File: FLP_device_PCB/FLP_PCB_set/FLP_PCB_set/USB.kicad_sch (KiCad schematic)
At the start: 2 parts, among them J1 USB_C_Receptacle_USB2.0_16P, U10 USBLC6-2P6

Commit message: FLP_set add
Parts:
- added C42: 22uF, Capacitor_SMD:C_0805_2012Metric, symbol Device:C
- J6: renamed from J1; footprint (none) -> 12402012E212A:AMPHENOL_12402012E212A
- renumbered U10 to U8
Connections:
- net 3.3V_USB: now also U8.5 (VBUS); no longer J6.A4_B9 (VBUS), J6.A9 (VBUS), J6.B4 (VBUS), J6.B4_A9 (VBUS), J6.B9 (VBUS)
- net GND: now also U8.2 (GND), C42.1
- new net 5V_USB: C42.2, J6.A4_B9 (VBUS), J6.A9 (VBUS), J6.B4 (VBUS), J6.B4_A9 (VBUS), J6.B9 (VBUS)

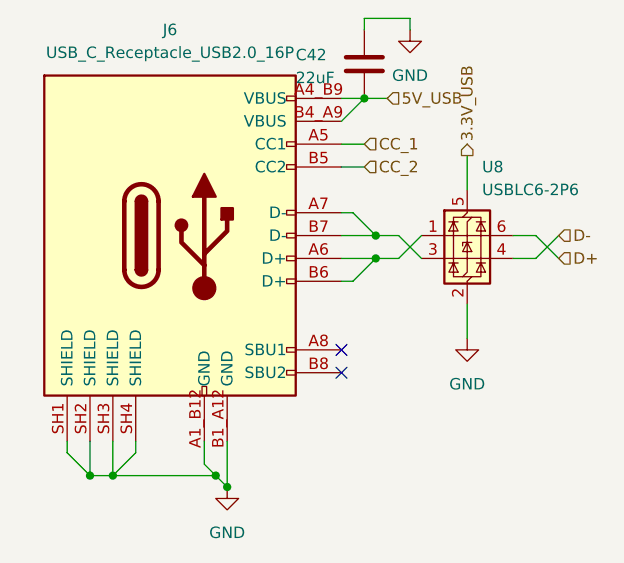
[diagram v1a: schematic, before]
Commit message: PCB fixing end adding description pdf
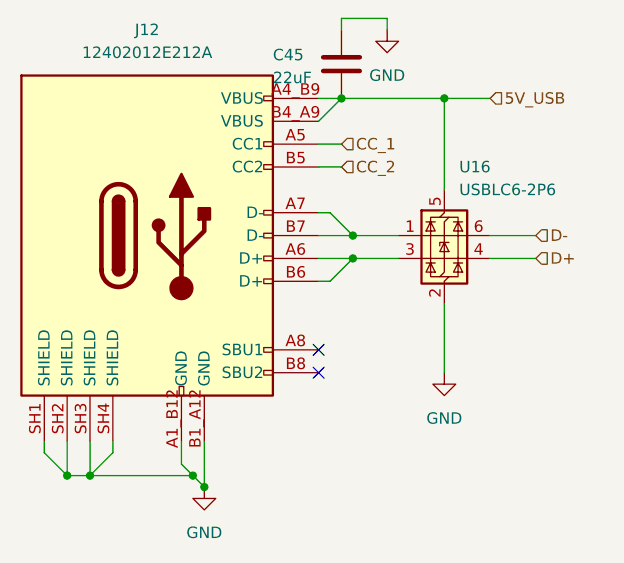
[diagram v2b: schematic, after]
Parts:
- removed C42: 22uF, Capacitor_SMD:C_0805_2012Metric, symbol Device:C
- removed J6: USB_C_Receptacle_USB2.0_16P, 12402012E212A:AMPHENOL_12402012E212A, symbol Connector:USB_C_Receptacle_USB2.0_16P
- removed U8: USBLC6-2P6, Package_TO_SOT_SMD:SOT-666, symbol Power_Protection:USBLC6-2P6
- added C45: 22uF, Capacitor_SMD:C_0805_2012Metric, symbol Device:C
- added J12: 12402012E212A, 12402012E212A:AMPHENOL_12402012E212A, symbol Connector:USB_C_Receptacle_USB2.0_16P
- added U16: USBLC6-2P6, Package_TO_SOT_SMD:SOT-666, symbol Power_Protection:USBLC6-2P6
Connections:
- net 5V_USB: now also C45.2, J12.A4_B9 (VBUS), J12.A9 (VBUS), J12.B4 (VBUS), J12.B4_A9 (VBUS), J12.B9 (VBUS), U16.5 (VBUS)
- net CC_1: now also J12.A5 (CC1)
- net CC_2: now also J12.B5 (CC2)
- net D+: now also U16.4 (I/O2)
- net D-: now also U16.6 (I/O1)
- net GND: now also C45.1, J12.A12 (GND), J12.A1_B12 (GND), J12.B1 (GND), J12.B12 (GND), J12.B1_A12 (GND), J12.SH1 (SHIELD), J12.SH2 (SHIELD), J12.SH3 (SHIELD), J12.SH4 (SHIELD), U16.2 (GND)
- new net: J12.A7 (D-), J12.B7 (D-), U16.1 (I/O1)
- new net: J12.A6 (D+), J12.B6 (D+), U16.3 (I/O2)
